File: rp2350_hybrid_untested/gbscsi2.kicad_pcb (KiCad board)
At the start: 4 copper layers, 69.5 x 93.5 mm, 147 parts, among them J1 USB_DATA, J2 TF003, J3 Conn_01x02, J4 Conn_01x04, J5 SCSI_50-2P_2mm, J6 SCSI_50P_2.54mm, J7 Conn_01x04, Q1 AO3401A, Q10 AO3401A, Q11 AO3401A, Q12 AO3401A, Q13 AO3401A, Q14 AO3401A, Q15 AO3401A, Q16 AO3401A, Q17 AO3401A, Q18 AO3401A, Q2 AO3401A, Q3 AO3401A, Q4 AO3401A, Q5 AO3401A, Q6 AO3401A, Q7 AO3401A, Q8 AO3401A, Q9 AO3401A, SW1 SW_DIP_x04, U1 RP2350_60QFN, U10 W25Q128JVS, U2 74LVT245, U3 74LVT245, U4 74AHCT1G125, U5 74LVT125, U6 74LVT125, U7 AZ1117-2.85, U8 AP62250WU, U9 USB TVS, Y1 12MHz

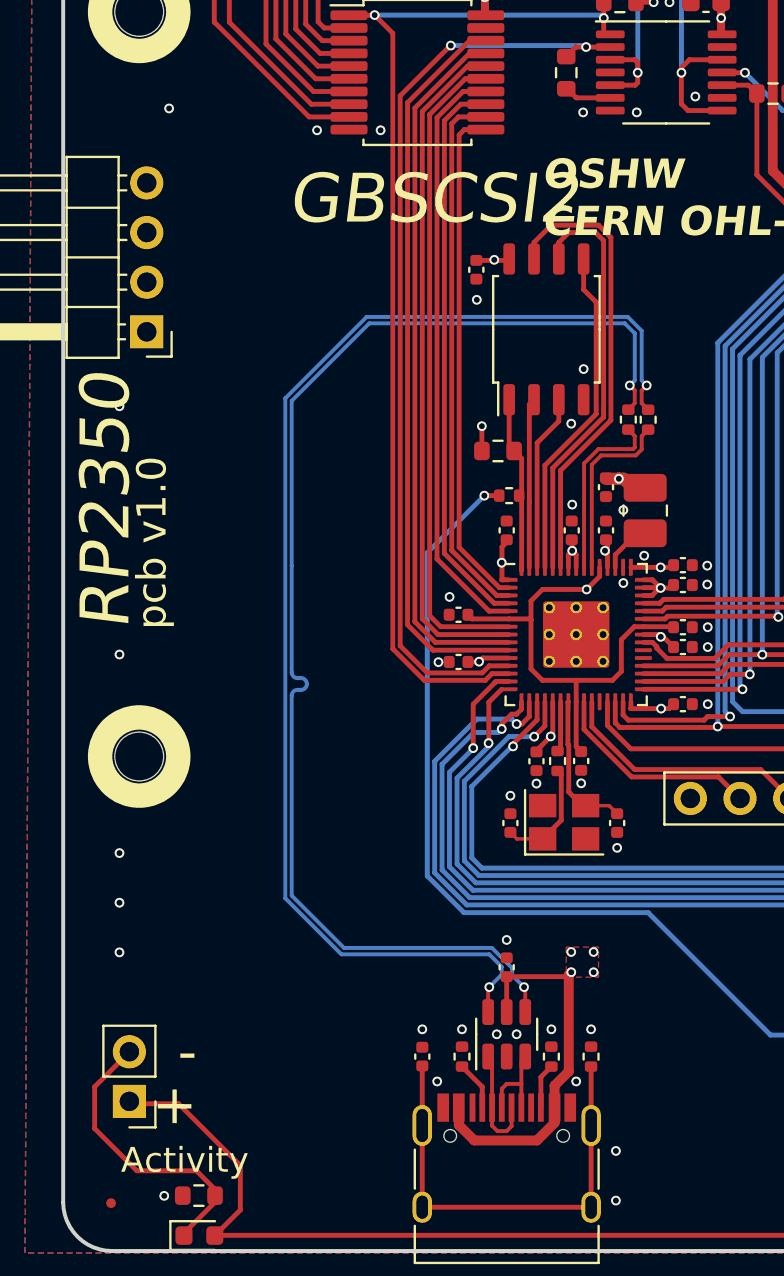
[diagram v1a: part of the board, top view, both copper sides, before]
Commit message: BoM fixes for discrete variants, interactive BoMs added to each major type, mfg files for 2350
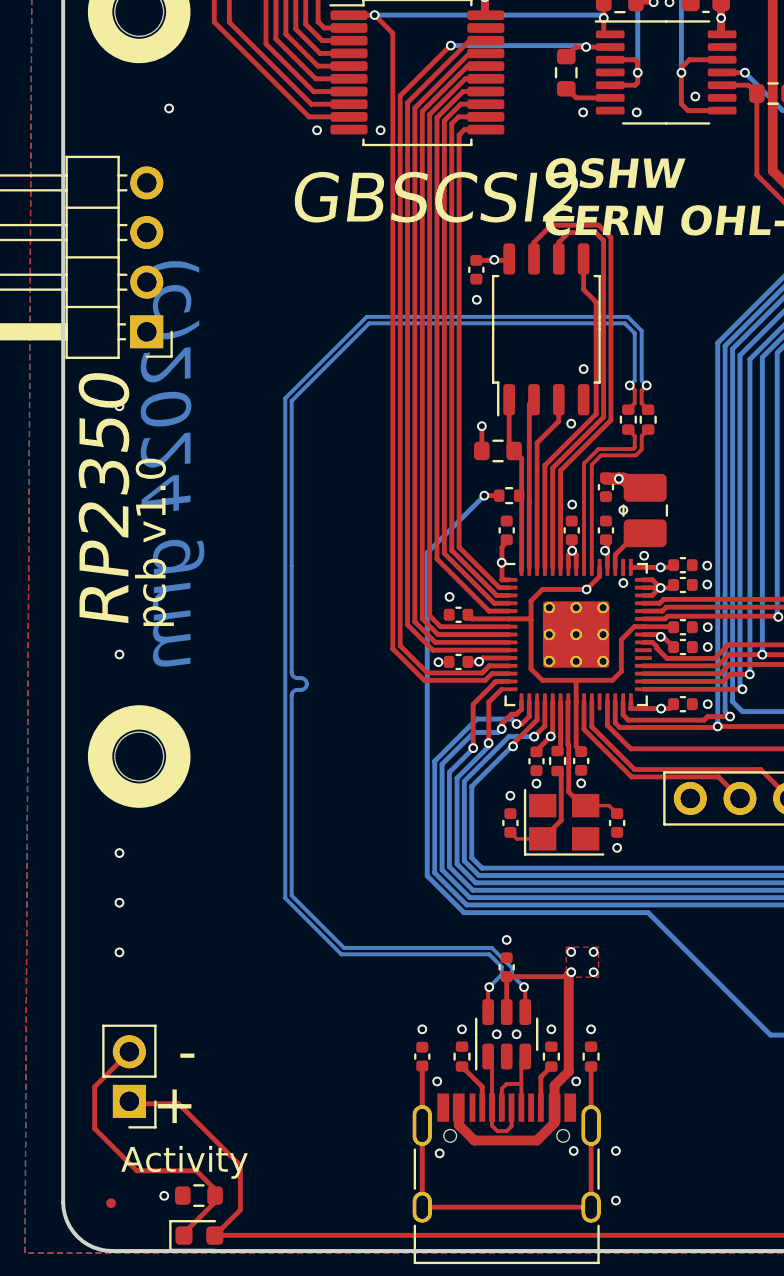
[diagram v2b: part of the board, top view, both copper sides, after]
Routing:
- net GND: vias 138 -> 140
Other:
- board text added: "(c)2024 grm"
